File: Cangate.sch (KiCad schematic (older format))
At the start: 0 parts

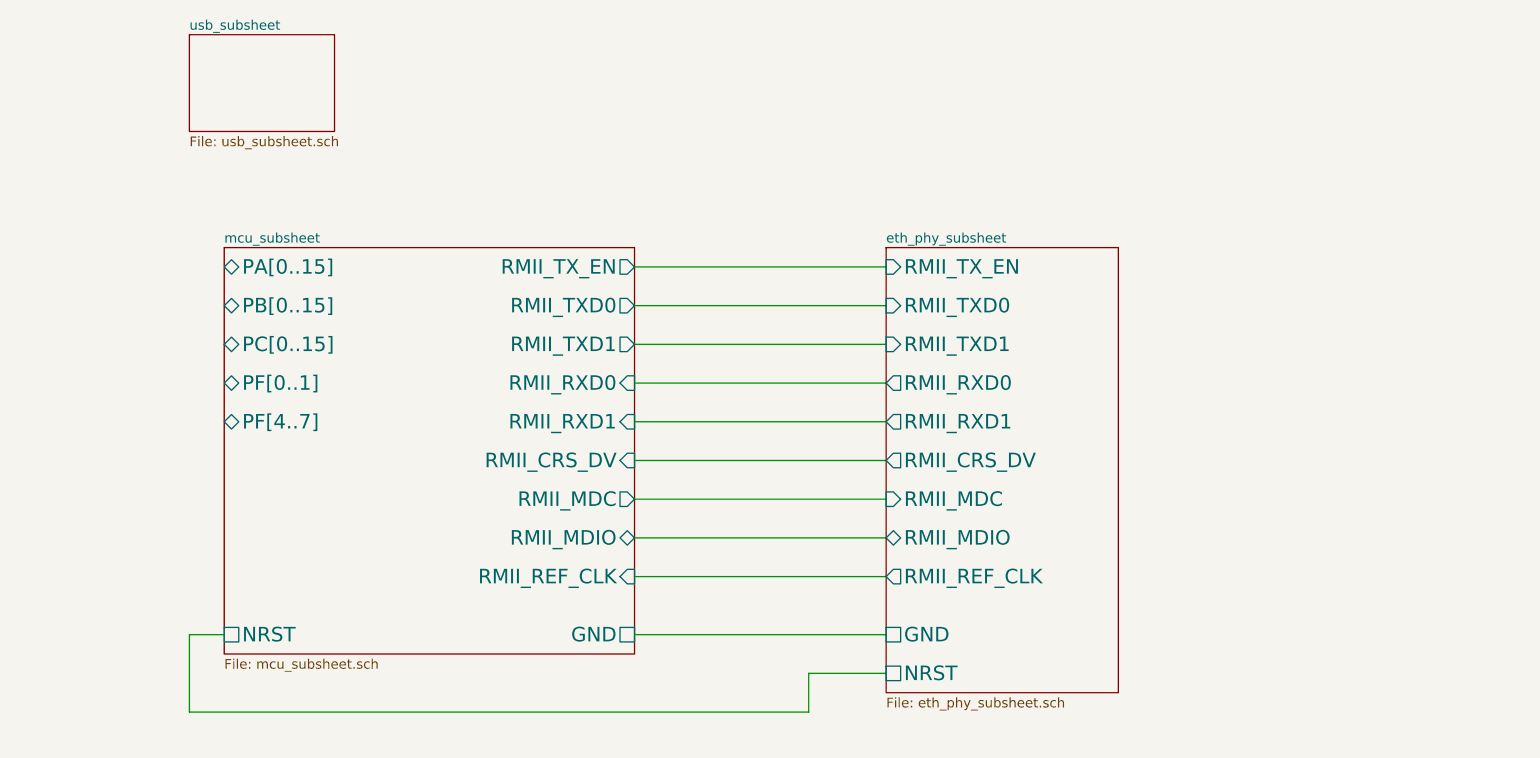
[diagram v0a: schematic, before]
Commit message: [usb]: wire isolator with dcdc + hierarchy
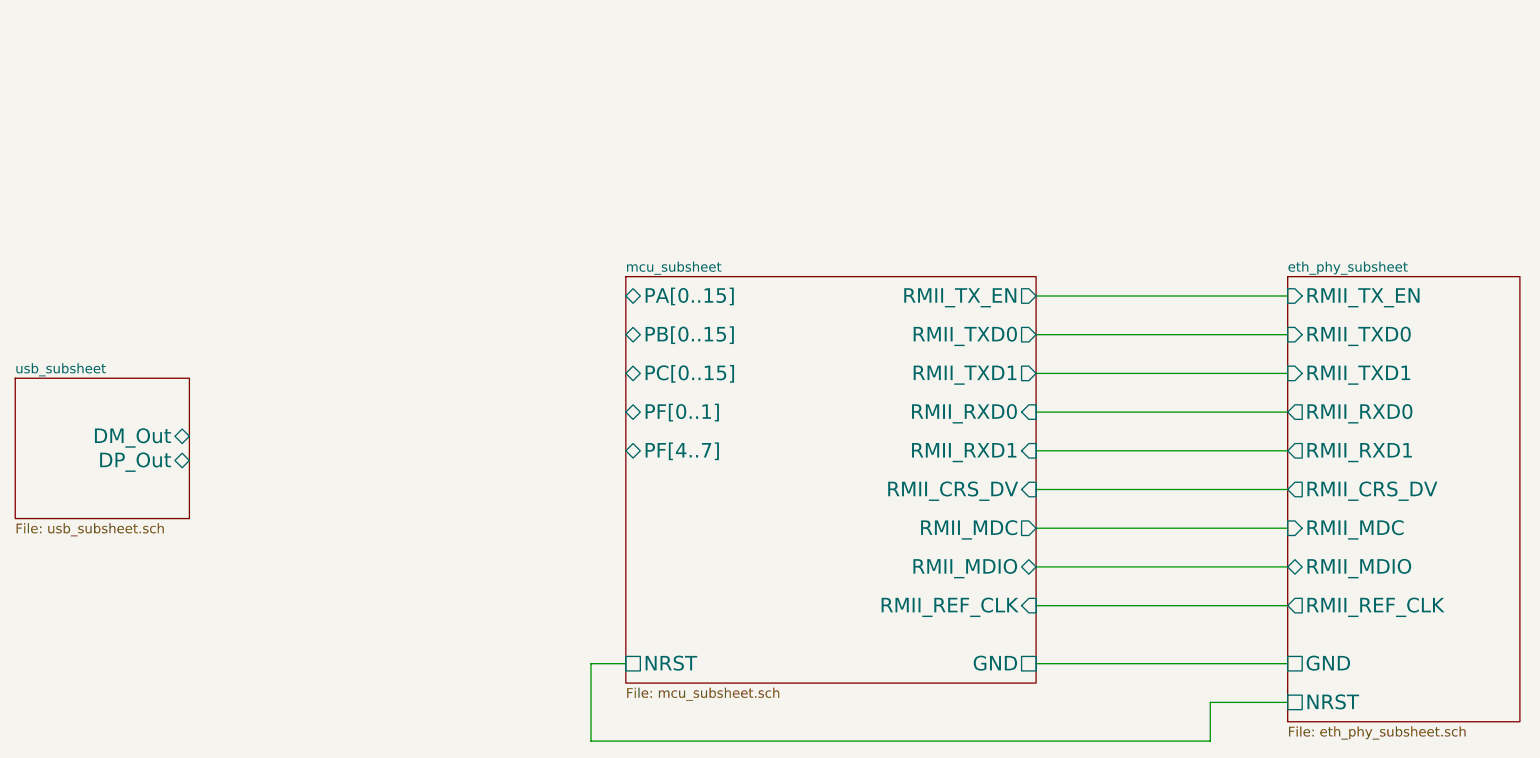
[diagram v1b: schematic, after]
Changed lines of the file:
@@
 $EndDescr
 $Sheet
-S 6100 2600 1200 2300
+S 8175 2750 1200 2300
 U 6176B826
 F0 "eth_phy_subsheet" 50
 F1 "eth_phy_subsheet.sch" 50
-F2 "RMII_TX_EN" I L 6100 2700 75
-F3 "RMII_TXD0" I L 6100 2900 75
-F4 "RMII_TXD1" I L 6100 3100 75
-F5 "RMII_RXD0" O L 6100 3300 75
-F6 "RMII_RXD1" O L 6100 3500 75
-F7 "RMII_CRS_DV" O L 6100 3700 75
-F8 "RMII_MDC" I L 6100 3900 75
-F9 "RMII_MDIO" B L 6100 4100 75
-F10 "RMII_REF_CLK" O L 6100 4300 75
-F11 "GND" U L 6100 4600 75
-F12 "NRST" U L 6100 4800 75
+F2 "RMII_TX_EN" I L 8175 2850 75
+F3 "RMII_TXD0" I L 8175 3050 75
+F4 "RMII_TXD1" I L 8175 3250 75
+F5 "RMII_RXD0" O L 8175 3450 75
+F6 "RMII_RXD1" O L 8175 3650 75
+F7 "RMII_CRS_DV" O L 8175 3850 75
+F8 "RMII_MDC" I L 8175 4050 75
+F9 "RMII_MDIO" B L 8175 4250 75
+F10 "RMII_REF_CLK" O L 8175 4450 75
+F11 "GND" U L 8175 4750 75
+F12 "NRST" U L 8175 4950 75
 $EndSheet
 $Sheet
-S 2680 2600 2120 2100
+S 4755 2750 2120 2100
 U 6176B761
 F0 "mcu_subsheet" 50
 F1 "mcu_subsheet.sch" 50
-F2 "RMII_TX_EN" O R 4800 2700 75
-F3 "RMII_TXD0" O R 4800 2900 75
-F4 "RMII_TXD1" O R 4800 3100 75
-F5 "RMII_RXD0" I R 4800 3300 75
-F6 "RMII_RXD1" I R 4800 3500 75
-F7 "RMII_CRS_DV" I R 4800 3700 75
-F8 "RMII_MDC" O R 4800 3900 75
-F9 "RMII_MDIO" B R 4800 4100 75
-F10 "RMII_REF_CLK" I R 4800 4300 75
-F11 "GND" U R 4800 4600 75
-F12 "NRST" U L 2680 4600 75
-F13 "PA[0..15]" B L 2680 2700 75
-F14 "PB[0..15]" B L 2680 2900 75
-F15 "PC[0..15]" B L 2680 3100 75
-F16 "PF[0..1]" B L 2680 3300 75
-F17 "PF[4..7]" B L 2680 3500 75
+F2 "RMII_TX_EN" O R 6875 2850 75
+F3 "RMII_TXD0" O R 6875 3050 75
+F4 "RMII_TXD1" O R 6875 3250 75
+F5 "RMII_RXD0" I R 6875 3450 75
+F6 "RMII_RXD1" I R 6875 3650 75
+F7 "RMII_CRS_DV" I R 6875 3850 75
+F8 "RMII_MDC" O R 6875 4050 75
+F9 "RMII_MDIO" B R 6875 4250 75
+F10 "RMII_REF_CLK" I R 6875 4450 75
+F11 "GND" U R 6875 4750 75
+F12 "NRST" U L 4755 4750 75
+F13 "PA[0..15]" B L 4755 2850 75
+F14 "PB[0..15]" B L 4755 3050 75
+F15 "PC[0..15]" B L 4755 3250 75
+F16 "PF[0..1]" B L 4755 3450 75
+F17 "PF[4..7]" B L 4755 3650 75
 $EndSheet
 Wire Wire Line
-	4800 2700 6100 2700
+	6875 2850 8175 2850
 Wire Wire Line
-	4800 2900 6100 2900
+	6875 3050 8175 3050
 Wire Wire Line
-	4800 3100 6100 3100
+	6875 3250 8175 3250
 Wire Wire Line
-	4800 3300 6100 3300
+	6875 3450 8175 3450
 Wire Wire Line
-	4800 3700 6100 3700
+	6875 3850 8175 3850
 Wire Wire Line
-	6100 3500 4800 3500
+	8175 3650 6875 3650
 Wire Wire Line
-	4800 3900 6100 3900
+	6875 4050 8175 4050
 Wire Wire Line
-	6100 4100 4800 4100
+	8175 4250 6875 4250
 Wire Wire Line
-	6100 4300 4800 4300
+	8175 4450 6875 4450
 Wire Wire Line
-	4800 4600 6100 4600
+	6875 4750 8175 4750
 Wire Wire Line
-	6100 4800 5700 4800
+	8175 4950 7775 4950
 Wire Wire Line
-	5700 4800 5700 5000
+	7775 4950 7775 5150
 Wire Wire Line
-	5700 5000 2500 5000
+	7775 5150 4575 5150
 Wire Wire Line
-	2500 5000 2500 4600
+	4575 5150 4575 4750
 Wire Wire Line
-	2500 4600 2680 4600
+	4575 4750 4755 4750
 $Sheet
-S 2500 1500 750  500
+S 1600 3275 900  725
 U 62087D00
 F0 "usb_subsheet" 50
 F1 "usb_subsheet.sch" 50
+F2 "DP_Out" B R 2500 3700 75
+F3 "DM_Out" B R 2500 3575 75
 $EndSheet
 $EndSCHEMATC
